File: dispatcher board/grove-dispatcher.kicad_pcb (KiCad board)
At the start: 2 copper layers, 158.8 x 77.5 mm, 54 parts, among them P1 CONN_01X05, P10 CONN_01X06, P11 CONN_01X05, P12 CONN_01X06, P13 CONN_01X06, P14 CONN_01X06, P15 CONN_01X06, P16 CONN_01X05, P17 CONN_01X06, P18 CONN_01X06, P19 CONN_01X06, P2 CONN_01X06, P20 CONN_01X06, P3 CONN_01X06, P4 CONN_01X06, P5 CONN_01X06, P6 CONN_01X05, P7 CONN_01X06, P8 CONN_01X06, P9 CONN_01X06, U1 PICO_BUCK, U2 PICO_BUCK, U3 PICO_BUCK, U4 PICO_BUCK

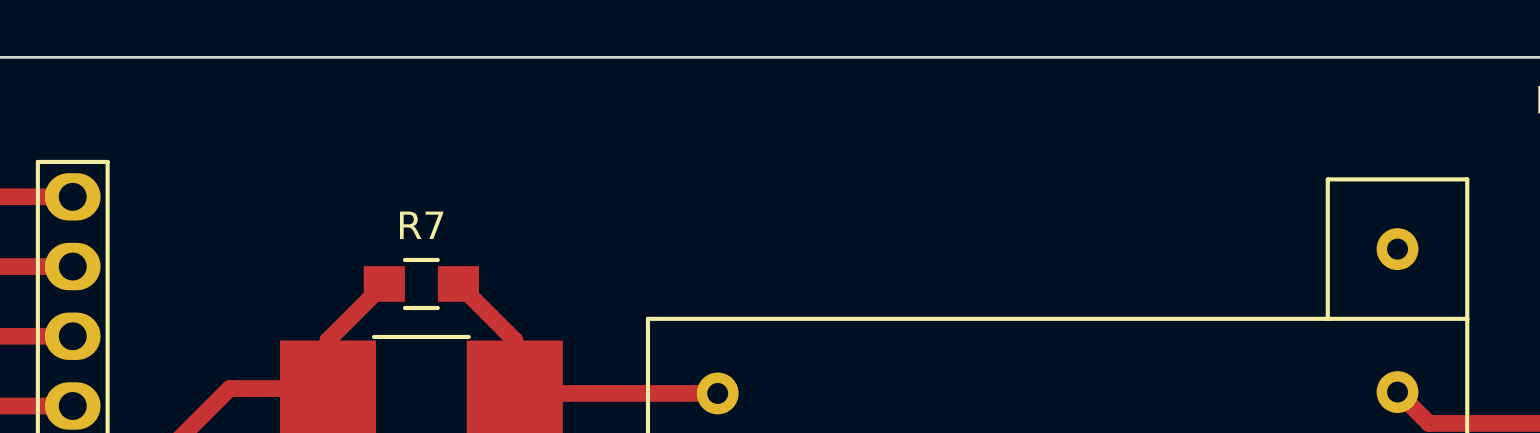
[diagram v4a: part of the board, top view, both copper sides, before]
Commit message: Add a silk screen with name and revision
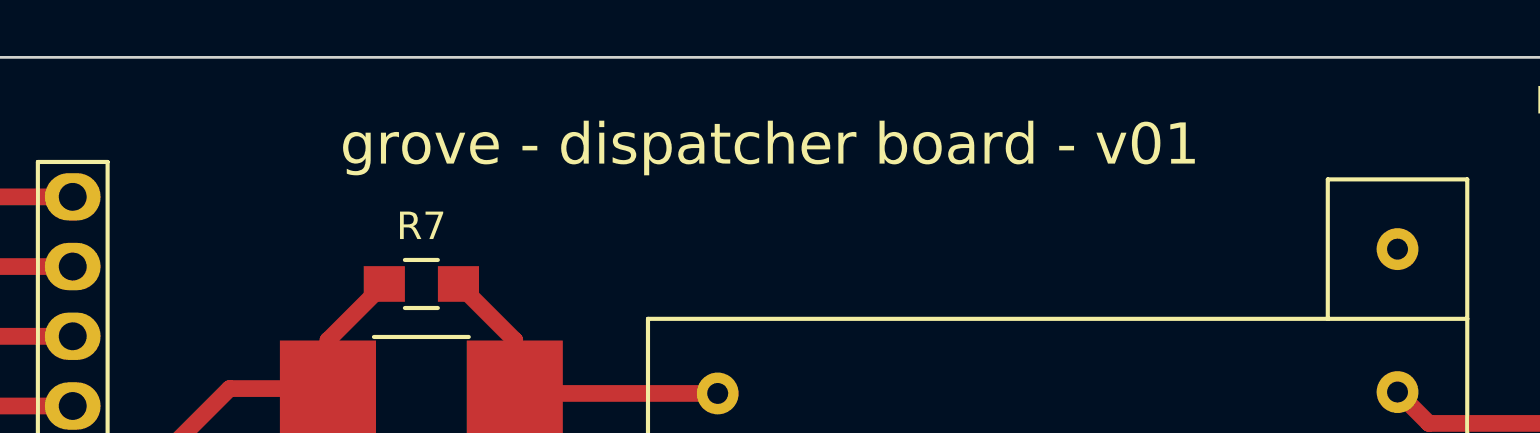
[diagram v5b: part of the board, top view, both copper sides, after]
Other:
- board text added: "grove - dispatcher board - v01"
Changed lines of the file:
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@@
     (links 159)
     (no_connects 0)
-    (area 0 0 0 0)
+    (area 67.996429 58.24 232.993572 135.960001)
     (thickness 1.6)
-    (drawings 5)
+    (drawings 6)
     (tracks 293)
     (zones 0)
@@
     (pad 1 np_thru_hole circle (at 0 0) (size 2.5 2.5) (drill 2.5) (layers *.Cu *.Mask F.SilkS))
   )
+  (gr_text "grove - dispatcher board - v01" (at 194.945 61.595) (layer F.SilkS)
+    (effects (font (size 1.5 1.5) (thickness 0.3)))
+  )
   (gr_line (start 71.12 135.89) (end 72.39 135.89) (angle 90) (layer Edge.Cuts) (width 0.1))

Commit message: Working on PCB some more
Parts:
- removed the P11 at (226.7, 81.9)
- removed the P16 at (226.7, 117.5)
- removed the P6 at (74.9, 72.4)
- removed REF** (x6): MountingHole_2.5mm, Mounting_Holes:MountingHole_2.5mm
- added C1: 1uF, Capacitors_SMD:C_0603_HandSoldering, F.Cu at (136.5, 121.9)
- added C2: 1uF, Capacitors_SMD:C_0603_HandSoldering, F.Cu at (136.5, 111.1)
- added C3: 1uF, Capacitors_SMD:C_0603_HandSoldering, F.Cu at (142.2, 111.1)
- added C4: 1uF, Capacitors_SMD:C_0603_HandSoldering, F.Cu at (142.2, 114.3)
- added R7: ?ohm, Resistors_SMD:R_0603_HandSoldering, F.Cu at (136.5, 119.4)
- added R8: ?ohms, Resistors_SMD:R_0603_HandSoldering, F.Cu at (142.2, 119.4)
- added U3: NCP603 ADJ / LD3985G25R, TO_SOT_Packages_SMD:SOT-23-5, F.Cu at (136.5, 115.6)
- added U5: BH2221FV, SMD_Packages:SSOP-20, F.Cu at (142.2, 105.4)
- P1: value CONN_01X05 -> CONN_01X12; footprint Pin_Headers:Pin_Header_Straight_1x05 -> Pin_Headers:Pin_Header_Straight_1x12
- moved P7 111.6 mm to (65.4, 116.2), turned to 0 degrees
- moved P3 109.8 mm to (65.4, 79.4), turned to 0 degrees
- moved P5 95.6 mm to (65.4, 61.0), turned to 0 degrees
- moved P10 94.4 mm to (214.6, 128.9), turned to 180 degrees
- moved U4 92.5 mm to (148.6, 126.4), turned to 90 degrees
- moved P6 88.3 mm to (78.1, 116.2), turned to 0 degrees
- moved P14 87.6 mm to (214.6, 92.1), turned to 180 degrees
- moved P2 86.1 mm to (78.1, 79.4), turned to 0 degrees
- moved P9 82.3 mm to (65.4, 97.8), turned to 0 degrees
- moved U1 81.9 mm to (131.4, 64.8), turned to 270 degrees
- moved P1 76.6 mm to (139.1, 68.6)
- moved P4 75.9 mm to (78.1, 61.0), turned to 0 degrees
- moved P17 74.9 mm to (214.6, 73.7), turned to 180 degrees
- moved P11 73.2 mm to (201.9, 128.9), turned to 180 degrees
- moved U6 72.9 mm to (148.6, 90.8), turned to 90 degrees
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- renumbered P12 to P10, P13 to P11, P14 to P12, P15 to P13, P17 to P14, P18 to P15, P19 to P16, P20 to P17, P7 to P6, P8 to P7, P9 to P8, P10 to P9, R8 to R10, R9 to R11, R10 to R12, R11 to R13, R12 to R14, R7 to R9, U3 to U4, U4 to U6
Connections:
- P1 pad 1: Net-(P1-Pad1) -> /V+
- P1 pad 2: Net-(P1-Pad2) -> /V+
- P1 pad 3: Net-(P1-Pad3) -> /V+
- P1 pad 4: GND -> /V+
- P1 pad 5: /V+ -> GND
- U1 pad 0: Net-(P1-Pad1) -> /AO1
- U1 pad 1: Net-(P1-Pad2) -> /AO2
- U1 pad 2: Net-(P1-Pad3) -> /AO3
- U2 pad 0: Net-(P6-Pad1) -> /AO4
- U2 pad 1: Net-(P6-Pad2) (its old number) -> /AO5
- U2 pad 2: Net-(P6-Pad3) -> /AO6
- U2 pad 5: Net-(P6-Pad5) -> /V+
- U4 pad 0: Net-(P11-Pad1) -> /AO7
- U4 pad 1: Net-(P11-Pad2) -> /AO8
- U4 pad 2: Net-(P11-Pad3) -> /AO9
- U4 pad 5: Net-(P11-Pad5) -> /V+
- U6 pad 0: Net-(P16-Pad1) -> /AO10
- U6 pad 1: Net-(P16-Pad2) -> /AO11
- U6 pad 2: Net-(P16-Pad3) -> /AO12
- U6 pad 5: Net-(P16-Pad5) -> /V+
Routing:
- net GND: track 54.9 -> 20.0 mm
- net Net-(P10-Pad6): track 62.7 -> 31.2 mm
- net Net-(P2-Pad6): track 62.7 -> 31.2 mm
- net Net-(P6-Pad6): track 65.8 -> 34.4 mm
- net Net-(P14-Pad6): track 63.7 -> 34.8 mm
- net Net-(F10-Pad2): track 61.2 -> 41.9 mm
- net Net-(F7-Pad2): track 60.8 -> 44.2 mm
- net Net-(P6-Pad4): track 66.9 -> 50.4 mm
- net Net-(F9-Pad2): track 53.5 -> 37.2 mm
- net Net-(F6-Pad2): track 53.5 -> 37.2 mm
- net Net-(F3-Pad2): track 53.5 -> 37.2 mm
- net Net-(P2-Pad4): track 66.9 -> 51.0 mm
- net Net-(F5-Pad2): track 57.1 -> 41.2 mm
- net Net-(F1-Pad2): track 58.9 -> 43.0 mm
- net Net-(P10-Pad4): track 65.7 -> 50.5 mm
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- removed copper zone on F.Cu, net GND
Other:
- board outline removed

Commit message: Did all the routing
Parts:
- moved C2 10.5 mm to (146.1, 115.6), turned to 90 degrees
- moved C1 5.72 mm to (142.2, 121.9)
- moved R7 5.72 mm to (142.2, 119.4)
- moved U3 5.72 mm to (142.2, 115.6)
- moved R8 5.08 mm to (137.2, 119.4), turned to 180 degrees
- moved C3 4.62 mm to (137.8, 109.9)
- moved C4 4.62 mm to (143.5, 109.9), turned to 180 degrees
- moved U5 2.69 mm to (140.3, 103.5)
- moved P1 1.27 mm to (140.3, 68.6)
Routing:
- net GND: track 20.0 -> 263.6 mm, vias 0 -> 5
- net /V+: track 0.00 -> 149.2 mm, vias 0 -> 1
- net +5V: track 0.00 -> 67.3 mm, vias 0 -> 1
- net Net-(P2-Pad6): track 31.2 -> 85.5 mm
- net Net-(P10-Pad6): track 31.2 -> 85.1 mm
- net Net-(P6-Pad6): track 34.4 -> 88.3 mm
- net Net-(P14-Pad6): track 34.8 -> 85.1 mm
- net /AO10: track 0.00 -> 49.3 mm, vias 0 -> 2
- net /AO11: track 0.00 -> 43.3 mm
- net /AO12: track 0.00 -> 34.8 mm
- net /AO4: track 0.00 -> 29.5 mm
- net +2V5: track 0.00 -> 26.9 mm, vias 0 -> 2
- net /AO7: track 0.00 -> 26.6 mm, vias 0 -> 1
- net /AO3: track 0.00 -> 26.6 mm
- net /AO5: track 0.00 -> 26.3 mm, vias 0 -> 1
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
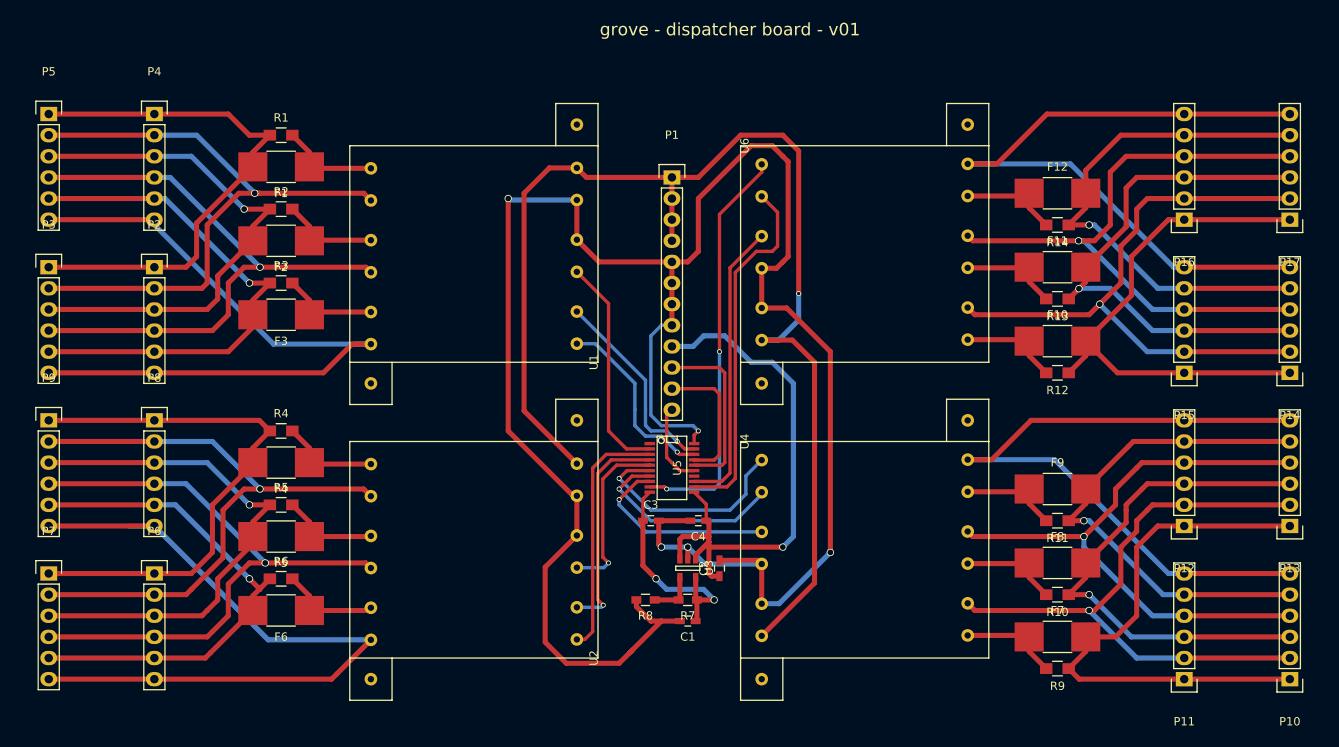
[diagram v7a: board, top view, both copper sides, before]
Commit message: Add edge cuts and zones
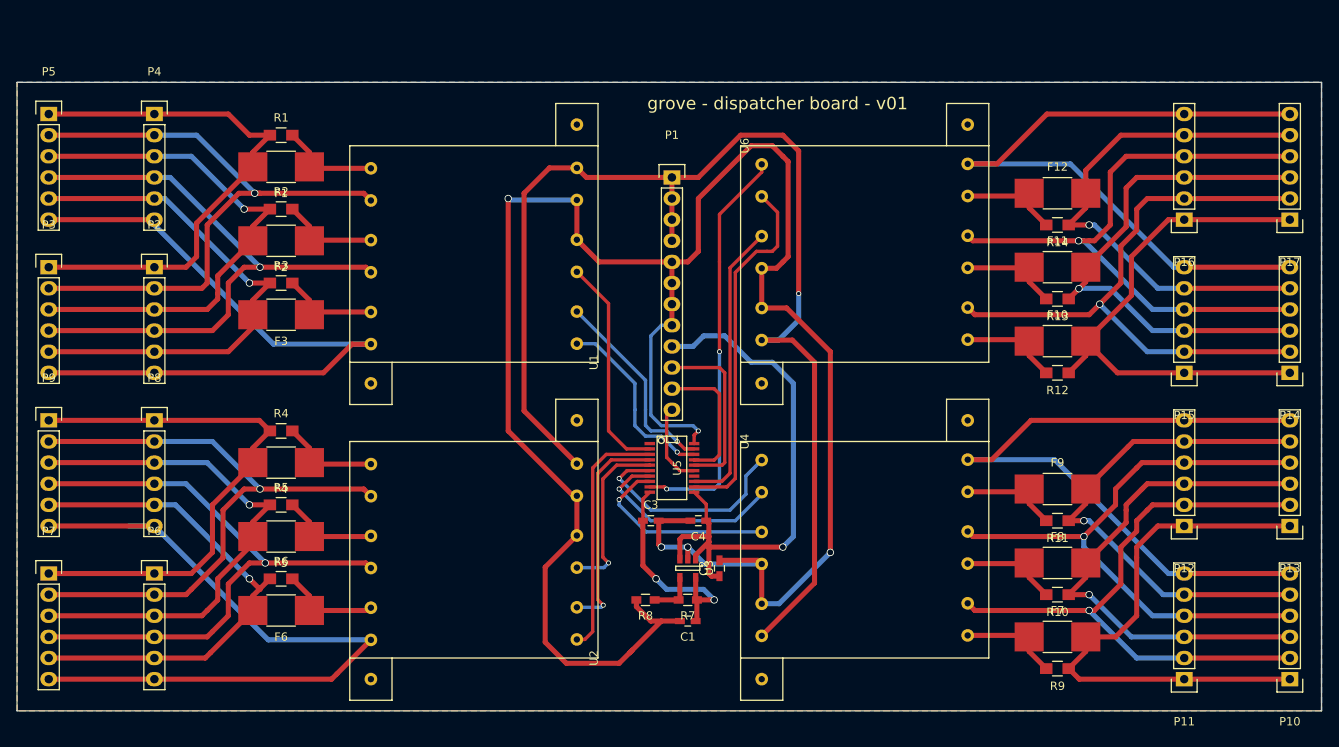
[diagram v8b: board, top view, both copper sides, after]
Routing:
- added copper zone on B.Cu, net GND
- added copper zone on F.Cu, net GND
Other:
- board outline added: 156.8 x 75.6 mm
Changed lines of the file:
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@@
     (links 183)
     (no_connects 0)
-    (area 60.296667 49.3 219.738334 134.98)
+    (area 60.296667 54.735 219.738334 134.98)
     (thickness 1.6)
-    (drawings 1)
+    (drawings 5)
     (tracks 578)
     (zones 0)
@@
     (pad_to_mask_clearance 0)
     (aux_axis_origin 0 0)
-    (grid_origin 118.11 109.22)
     (visible_elements FFFFFF7F)
     (pcbplotparams
@@
     )
   )
-  (gr_text "grove - dispatcher board - v01" (at 147.32 50.8) (layer F.SilkS)
+  (gr_line (start 61.595 132.715) (end 218.44 132.715) (angle 90) (layer Edge.Cuts) (width 0.1))
+  (gr_line (start 61.595 57.15) (end 61.595 132.715) (angle 90) (layer Edge.Cuts) (width 0.1))
+  (gr_line (start 218.44 57.15) (end 61.595 57.15) (angle 90) (layer Edge.Cuts) (width 0.1))
+  (gr_line (start 218.44 132.715) (end 218.44 57.15) (angle 90) (layer Edge.Cuts) (width 0.1))
+  (gr_text "grove - dispatcher board - v01" (at 153.035 59.69) (layer F.SilkS)
     (effects (font (size 1.5 1.5) (thickness 0.3)))
   )
@@
   (segment (start 147.32 104.14) (end 147.32 79.4512) (width 0.4064) (layer F.Cu) (net 56))
   (segment (start 146.3294 105.1306) (end 147.32 104.14) (width 0.4064) (layer F.Cu) (net 56))
+  (zone (net 26) (net_name GND) (layer F.Cu) (hatch edge 0.508)
+    (connect_pads (clearance 0.508))
+    (min_thickness 0.254)
+    (fill yes (arc_segments 16) (thermal_gap 0.508) (thermal_bridge_width 0.508))
+    (polygon
+      (pts
+        (xy 218.44 132.715) (xy 61.595 132.715) (xy 61.595 57.15) (xy 218.44 57.15) (xy 218.44 132.715)
+      )
+    )
+  )
+  (zone (net 26) (net_name GND) (layer B.Cu) (hatch edge 0.508)
+    (connect_pads (clearance 0.508))
+    (min_thickness 0.254)
+    (fill yes (arc_segments 16) (thermal_gap 0.508) (thermal_bridge_width 0.508))
+    (polygon
+      (pts
+        (xy 218.44 132.715) (xy 61.595 132.715) (xy 61.595 57.15) (xy 218.44 57.15) (xy 218.44 132.715)
+      )
+    )
+  )
 )
